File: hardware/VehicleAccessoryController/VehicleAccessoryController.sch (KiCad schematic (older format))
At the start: 70 parts, among them J501 Input, J502 Front Conn, J503 Rear Conn, J504 Left Conn, J505 Right Conn, J506 USB_B_Mini, P601 TC2030-MCP, Q201 BSS138, Q202 BSS138, Q203 BSS138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

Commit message: schematic updates
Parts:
- added C812, C813: 0.1uF, VehicleAccessoryController:C_0603, symbol Device:C
- added U106: Si8621BB-B-IS, Package_SO:SOIC-8_3.9x4.9mm_P1.27mm, symbol VehicleAccessoryController:Si8621BB-B-IS
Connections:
- net +5V: now also C813.1, U106.8 (VDD2)
- net CTRL: now also SW301.2 (B)
- net GND: now also C813.2, U106.5 (GND2); no longer C810.2, D605.1 (A), J506.5 (GND), R727.1, R732.1, U105.2 (GND), U105.25 (GND)
- net VDD: now also C812.1, U106.1 (VDD1)
- net CP2102N_RXD: now reaches U105.20 (RXD)
- net CP2102N_RXD: now also U106.3 (A2)
- net UART_RXD renamed 328P_RXD
- net 328P_RXD: now also U106.7 (B1); no longer U105.21 (TXD)
- net UART_TXD renamed 328P_TXD
- net 328P_TXD: now also U106.6 (B2)
- new net CP2102N_TXD: U105.21 (TXD), U106.2 (A1)
- new net GNDD: C810.2, C812.2, D605.1 (A), J506.5 (GND), R727.1, R732.1, U105.2 (GND), U105.25 (GND), U106.4 (GND1)
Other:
- moved on the sheet: C802, C803, C810, C811, D605, J506, P601, R702, R705, R727, R728, R731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

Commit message: test board schematic/layout updates, gerbers
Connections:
- net GND: no longer C806.2, C807.2, C808.2, C809.2
- net GNDD: now also C806.2, C807.2, C808.2, C809.2
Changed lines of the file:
@@
 Sheet 1 1
 Title "Vehicle Accessory Controller"
-Date "2019-10-31"
+Date "2019-11-15"
 Rev "0.1"
 Comp "Noctivore"
@@
 	1    0    0    -1
 $EndComp
-$Comp
-L power:GND #PWR0149
-U 1 1 5DC4B377
-P 4450 7275
-F 0 "#PWR0149" H 4450 7025 50  0001 C CNN
-F 1 "GND" H 4455 7102 50  0000 C CNN
-F 2 "" H 4450 7275 50  0001 C CNN
-F 3 "" H 4450 7275 50  0001 C CNN
-	1    4450 7275
-	1    0    0    -1
-$EndComp
-$Comp
-L power:GND #PWR0150
-U 1 1 5DC546B1
-P 4900 7275
-F 0 "#PWR0150" H 4900 7025 50  0001 C CNN
-F 1 "GND" H 4905 7102 50  0000 C CNN
-F 2 "" H 4900 7275 50  0001 C CNN
-F 3 "" H 4900 7275 50  0001 C CNN
-	1    4900 7275
-	1    0    0    -1
-$EndComp
 Wire Wire Line
 	4450 6825 4450 6900
@@
 F 3 "" H 5850 6825 50  0001 C CNN
 	1    5850 6825
-	1    0    0    -1
-$EndComp
-$Comp
-L power:GND #PWR0154
-U 1 1 5DCBD7D2
-P 5400 7275
-F 0 "#PWR0154" H 5400 7025 50  0001 C CNN
-F 1 "GND" H 5405 7102 50  0000 C CNN
-F 2 "" H 5400 7275 50  0001 C CNN
-F 3 "" H 5400 7275 50  0001 C CNN
-	1    5400 7275
-	1    0    0    -1
-$EndComp
-$Comp
-L power:GND #PWR0155
-U 1 1 5DCBD7D8
-P 5850 7275
-F 0 "#PWR0155" H 5850 7025 50  0001 C CNN
-F 1 "GND" H 5855 7102 50  0000 C CNN
-F 2 "" H 5850 7275 50  0001 C CNN
-F 3 "" H 5850 7275 50  0001 C CNN
-	1    5850 7275
 	1    0    0    -1
 $EndComp
@@
 Wire Wire Line
 	3500 1850 3500 1925
+$Comp
+L power:GNDD #PWR0149
+U 1 1 5DD0CEEA
+P 4450 7275
+F 0 "#PWR0149" H 4450 7025 50  0001 C CNN
+F 1 "GNDD" H 4454 7120 50  0000 C CNN
+F 2 "" H 4450 7275 50  0001 C CNN
+F 3 "" H 4450 7275 50  0001 C CNN
+	1    4450 7275
+	1    0    0    -1
+$EndComp
+$Comp
+L power:GNDD #PWR0150
+U 1 1 5DD13D48
+P 4900 7275
+F 0 "#PWR0150" H 4900 7025 50  0001 C CNN
+F 1 "GNDD" H 4904 7120 50  0000 C CNN
+F 2 "" H 4900 7275 50  0001 C CNN
+F 3 "" H 4900 7275 50  0001 C CNN
+	1    4900 7275
+	1    0    0    -1
+$EndComp
+$Comp
+L power:GNDD #PWR0154
+U 1 1 5DD1425B
+P 5400 7275
+F 0 "#PWR0154" H 5400 7025 50  0001 C CNN
+F 1 "GNDD" H 5404 7120 50  0000 C CNN
+F 2 "" H 5400 7275 50  0001 C CNN
+F 3 "" H 5400 7275 50  0001 C CNN
+	1    5400 7275
+	1    0    0    -1
+$EndComp
+$Comp
+L power:GNDD #PWR0155
+U 1 1 5DD1473A
+P 5850 7275
+F 0 "#PWR0155" H 5850 7025 50  0001 C CNN
+F 1 "GNDD" H 5854 7120 50  0000 C CNN
+F 2 "" H 5850 7275 50  0001 C CNN
+F 3 "" H 5850 7275 50  0001 C CNN
+	1    5850 7275
+	1    0    0    -1
+$EndComp
 $EndSCHEMATC

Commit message: BOM update, change output connectors
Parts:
- J502, J503, J504, J505: footprint VehicleAccessoryController:Keystone_8719 -> VehicleAccessoryController:TE_1776275-3
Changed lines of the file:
@@
 F 0 "J502" H 10050 1250 50  0000 L CNN
 F 1 "Front Conn" V 10275 850 50  0000 L CNN
-F 2 "VehicleAccessoryController:Keystone_8719" H 10175 1050 50  0001 C CNN
+F 2 "VehicleAccessoryController:TE_1776275-3" H 10175 1050 50  0001 C CNN
 F 3 "~" H 10175 1050 50  0001 C CNN
 	1    10175 1050
@@
 F 0 "J503" H 10050 2750 50  0000 L CNN
 F 1 "Rear Conn" V 10275 2375 50  0000 L CNN
-F 2 "VehicleAccessoryController:Keystone_8719" H 10175 2550 50  0001 C CNN
+F 2 "VehicleAccessoryController:TE_1776275-3" H 10175 2550 50  0001 C CNN
 F 3 "~" H 10175 2550 50  0001 C CNN
 	1    10175 2550
@@
 F 0 "J504" H 10050 4250 50  0000 L CNN
 F 1 "Left Conn" V 10275 3875 50  0000 L CNN
-F 2 "VehicleAccessoryController:Keystone_8719" H 10175 4050 50  0001 C CNN
+F 2 "VehicleAccessoryController:TE_1776275-3" H 10175 4050 50  0001 C CNN
 F 3 "~" H 10175 4050 50  0001 C CNN
 	1    10175 4050
@@
 F 0 "J505" H 10050 5750 50  0000 L CNN
 F 1 "Right Conn" V 10275 5325 50  0000 L CNN
-F 2 "VehicleAccessoryController:Keystone_8719" H 10175 5550 50  0001 C CNN
+F 2 "VehicleAccessoryController:TE_1776275-3" H 10175 5550 50  0001 C CNN
 F 3 "~" H 10175 5550 50  0001 C CNN
 	1    10175 5550

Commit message: schematic updates, begin layout
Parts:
- J506: symbol Connector:USB_B_Mini -> VehicleAccessoryController:USB_Mini-B
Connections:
- net +5V: no longer C802.1, C805.1, C813.1, D601.2 (A), D602.2 (A), P601.1 (MCLR/Vpp), R702.1, R726.1, U102.18 (AVCC), U102.4 (VCC), U104.8 (VDD), U106.8 (VDD2)
- net SHIELD: now also J506.0 (Shield); no longer J506.6 (Shield)
- new net +5VD: C802.1, C805.1, C813.1, D601.2 (A), D602.2 (A), P601.1 (MCLR/Vpp), R702.1, R726.1, U102.18 (AVCC), U102.4 (VCC), U104.8 (VDD), U106.8 (VDD2)
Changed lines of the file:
@@
 EESchema Schematic File Version 4
-LIBS:VehicleAccessoryController-cache
 EELAYER 30 0
 EELAYER END
@@
 Sheet 1 1
 Title "Vehicle Accessory Controller"
-Date "2019-11-15"
+Date "2019-11-20"
 Rev "0.1"
 Comp "Noctivore"
@@
 	1    0    0    -1
 $EndComp
-$Comp
-L power:+5V #PWR0103
-U 1 1 5DAF83B3
-P 5675 775
-F 0 "#PWR0103" H 5675 625 50  0001 C CNN
-F 1 "+5V" H 5690 948 50  0000 C CNN
-F 2 "" H 5675 775 50  0001 C CNN
-F 3 "" H 5675 775 50  0001 C CNN
-	1    5675 775
-	1    0    0    -1
-$EndComp
 Text Label 6525 2075 0    50   ~ 0
 328P_MOSI
@@
 	1    0    0    -1
 $EndComp
-$Comp
-L power:+5V #PWR0104
-U 1 1 5DAF8DA2
-P 4825 1175
-F 0 "#PWR0104" H 4825 1025 50  0001 C CNN
-F 1 "+5V" H 4840 1348 50  0000 C CNN
-F 2 "" H 4825 1175 50  0001 C CNN
-F 3 "" H 4825 1175 50  0001 C CNN
-	1    4825 1175
-	1    0    0    -1
-$EndComp
 Wire Wire Line
 	4825 1175 4825 1275
@@
 Wire Wire Line
 	4825 1775 4975 1775
-$Comp
-L power:+5V #PWR0105
-U 1 1 5DAF8FC6
-P 4525 1175
-F 0 "#PWR0105" H 4525 1025 50  0001 C CNN
-F 1 "+5V" H 4540 1348 50  0000 C CNN
-F 2 "" H 4525 1175 50  0001 C CNN
-F 3 "" H 4525 1175 50  0001 C CNN
-	1    4525 1175
-	1    0    0    -1
-$EndComp
 Wire Wire Line
 	4525 1175 4525 1875
@@
 F 3 "~" H 4225 1425 50  0001 C CNN
 	1    4225 1425
-	1    0    0    -1
-$EndComp
-$Comp
-L power:+5V #PWR0107
-U 1 1 5DAF9C6A
-P 4225 1175
-F 0 "#PWR0107" H 4225 1025 50  0001 C CNN
-F 1 "+5V" H 4240 1348 50  0000 C CNN
-F 2 "" H 4225 1175 50  0001 C CNN
-F 3 "" H 4225 1175 50  0001 C CNN
-	1    4225 1175
 	1    0    0    -1
 $EndComp
@@
 $EndComp
 $Comp
-L power:+5V #PWR05
-U 1 1 5DB32CA0
-P 2175 6825
-F 0 "#PWR05" H 2175 6675 50  0001 C CNN
-F 1 "+5V" H 2190 6998 50  0000 C CNN
-F 2 "" H 2175 6825 50  0001 C CNN
-F 3 "" H 2175 6825 50  0001 C CNN
-	1    2175 6825
-	1    0    0    -1
-$EndComp
-$Comp
 L Device:R R706
 U 1 1 5DB32F81
@@
 $EndComp
 $Comp
-L power:+5V #PWR0130
-U 1 1 5DB94CF1
-P 2425 5525
-F 0 "#PWR0130" H 2425 5375 50  0001 C CNN
-F 1 "+5V" H 2440 5698 50  0000 C CNN
-F 2 "" H 2425 5525 50  0001 C CNN
-F 3 "" H 2425 5525 50  0001 C CNN
-	1    2425 5525
-	1    0    0    -1
-$EndComp
-$Comp
 L power:GND #PWR0131
 U 1 1 5DB94D36
@@
 F 3 "~" H 1875 7450 50  0001 C CNN
 	1    1875 7450
-	1    0    0    -1
-$EndComp
-$Comp
-L power:+5V #PWR0140
-U 1 1 5DC8A8AF
-P 2175 7375
-F 0 "#PWR0140" H 2175 7225 50  0001 C CNN
-F 1 "+5V" H 2190 7548 50  0000 C CNN
-F 2 "" H 2175 7375 50  0001 C CNN
-F 3 "" H 2175 7375 50  0001 C CNN
-	1    2175 7375
 	1    0    0    -1
 $EndComp
@@
 	6925 1325 6925 1400
 $Comp
-L Connector:USB_B_Mini J506
+L VehicleAccessoryController:USB_Mini-B J506
 U 1 1 5DC3DA46
 P 5100 5775
@@
 $EndComp
 $Comp
-L power:+5V #PWR0144
-U 1 1 5DC3FCB0
-P 3525 5525
-F 0 "#PWR0144" H 3525 5375 50  0001 C CNN
-F 1 "+5V" H 3540 5698 50  0000 C CNN
-F 2 "" H 3525 5525 50  0001 C CNN
-F 3 "" H 3525 5525 50  0001 C CNN
-	1    3525 5525
-	1    0    0    -1
-$EndComp
-$Comp
 L power:GND #PWR0145
 U 1 1 5DC3FCB6
@@
 Wire Wire Line
 	3525 5900 3525 5975
-$Comp
-L power:+5V #PWR0146
-U 1 1 5DC61045
-P 3075 5525
-F 0 "#PWR0146" H 3075 5375 50  0001 C CNN
-F 1 "+5V" H 3090 5698 50  0000 C CNN
-F 2 "" H 3075 5525 50  0001 C CNN
-F 3 "" H 3075 5525 50  0001 C CNN
-	1    3075 5525
-	1    0    0    -1
-$EndComp
 Wire Wire Line
 	3075 5600 3075 5525
@@
 $EndComp
 $Comp
-L power:+5V #PWR0158
-U 1 1 5DD3D68A
-P 6800 3700
-F 0 "#PWR0158" H 6800 3550 50  0001 C CNN
-F 1 "+5V" H 6815 3873 50  0000 C CNN
-F 2 "" H 6800 3700 50  0001 C CNN
-F 3 "" H 6800 3700 50  0001 C CNN
-	1    6800 3700
-	1    0    0    -1
-$EndComp
-$Comp
 L power:GNDD #PWR0159
 U 1 1 5DD484EB
@@
 $EndComp
 $Comp
-L power:+5V #PWR0173
-U 1 1 5DD89F10
-P 7325 3700
-F 0 "#PWR0173" H 7325 3550 50  0001 C CNN
-F 1 "+5V" H 7340 3873 50  0000 C CNN
-F 2 "" H 7325 3700 50  0001 C CNN
-F 3 "" H 7325 3700 50  0001 C CNN
-	1    7325 3700
-	1    0    0    -1
-$EndComp
-$Comp
 L power:GND #PWR0174
 U 1 1 5DD89F1A
@@
 	1    0    0    -1
 $EndComp
+$Comp
+L power:+5VD #PWR0103
+U 1 1 5DDD65F9
+P 7575 2200
+F 0 "#PWR0103" H 7575 2050 50  0001 C CNN
+F 1 "+5VD" H 7590 2373 50  0000 C CNN
+F 2 "" H 7575 2200 50  0001 C CNN
+F 3 "" H 7575 2200 50  0001 C CNN
+	1    7575 2200
+	1    0    0    -1
+$EndComp
+$Comp
+L power:+5V #PWR0104
+U 1 1 5DDD6A05
+P 7350 2200
+F 0 "#PWR0104" H 7350 2050 50  0001 C CNN
+F 1 "+5V" H 7365 2373 50  0000 C CNN
+F 2 "" H 7350 2200 50  0001 C CNN
+F 3 "" H 7350 2200 50  0001 C CNN
+	1    7350 2200
+	1    0    0    -1
+$EndComp
+$Comp
+L power:+5VD #PWR0105
+U 1 1 5DDD71B1
+P 4225 1175
+F 0 "#PWR0105" H 4225 1025 50  0001 C CNN
+F 1 "+5VD" H 4240 1348 50  0000 C CNN
+F 2 "" H 4225 1175 50  0001 C CNN
+F 3 "" H 4225 1175 50  0001 C CNN
+	1    4225 1175
+	1    0    0    -1
+$EndComp
+$Comp
+L power:+5VD #PWR0107
+U 1 1 5DDD7521
+P 4525 1175
+F 0 "#PWR0107" H 4525 1025 50  0001 C CNN
+F 1 "+5VD" H 4540 1348 50  0000 C CNN
+F 2 "" H 4525 1175 50  0001 C CNN
+F 3 "" H 4525 1175 50  0001 C CNN
+	1    4525 1175
+	1    0    0    -1
+$EndComp
+$Comp
+L power:+5VD #PWR0130
+U 1 1 5DDD788E
+P 4825 1175
+F 0 "#PWR0130" H 4825 1025 50  0001 C CNN
+F 1 "+5VD" H 4840 1348 50  0000 C CNN
+F 2 "" H 4825 1175 50  0001 C CNN
+F 3 "" H 4825 1175 50  0001 C CNN
+	1    4825 1175
+	1    0    0    -1
+$EndComp
+$Comp
+L power:+5VD #PWR0140
+U 1 1 5DDD7BAE
+P 5675 775
+F 0 "#PWR0140" H 5675 625 50  0001 C CNN
+F 1 "+5VD" H 5690 948 50  0000 C CNN
+F 2 "" H 5675 775 50  0001 C CNN
+F 3 "" H 5675 775 50  0001 C CNN
+	1    5675 775
+	1    0    0    -1
+$EndComp
+$Comp
+L power:+5VD #PWR0144
+U 1 1 5DDE8D2C
+P 7325 3700
+F 0 "#PWR0144" H 7325 3550 50  0001 C CNN
+F 1 "+5VD" H 7340 3873 50  0000 C CNN
+F 2 "" H 7325 3700 50  0001 C CNN
+F 3 "" H 7325 3700 50  0001 C CNN
+	1    7325 3700
+	1    0    0    -1
+$EndComp
+$Comp
+L power:+5VD #PWR0146
+U 1 1 5DDEA530
+P 6800 3700
+F 0 "#PWR0146" H 6800 3550 50  0001 C CNN
+F 1 "+5VD" H 6815 3873 50  0000 C CNN
+F 2 "" H 6800 3700 50  0001 C CNN
+F 3 "" H 6800 3700 50  0001 C CNN
+	1    6800 3700
+	1    0    0    -1
+$EndComp
+$Comp
+L power:+5VD #PWR0158
+U 1 1 5DDF1341
+P 2425 5525
+F 0 "#PWR0158" H 2425 5375 50  0001 C CNN
+F 1 "+5VD" H 2440 5698 50  0000 C CNN
+F 2 "" H 2425 5525 50  0001 C CNN
+F 3 "" H 2425 5525 50  0001 C CNN
+	1    2425 5525
+	1    0    0    -1
+$EndComp
+$Comp
+L power:+5VD #PWR0173
+U 1 1 5DDF3D8B
+P 3075 5525
+F 0 "#PWR0173" H 3075 5375 50  0001 C CNN
+F 1 "+5VD" H 3090 5698 50  0000 C CNN
+F 2 "" H 3075 5525 50  0001 C CNN
+F 3 "" H 3075 5525 50  0001 C CNN
+	1    3075 5525
+	1    0    0    -1
+$EndComp
+$Comp
+L power:+5VD #PWR0177
+U 1 1 5DDF3FF7
+P 3525 5525
+F 0 "#PWR0177" H 3525 5375 50  0001 C CNN
+F 1 "+5VD" H 3540 5698 50  0000 C CNN
+F 2 "" H 3525 5525 50  0001 C CNN
+F 3 "" H 3525 5525 50  0001 C CNN
+	1    3525 5525
+	1    0    0    -1
+$EndComp
+$Comp
+L power:GND #PWR0178
+U 1 1 5DDF795F
+P 7475 2325
+F 0 "#PWR0178" H 7475 2075 50  0001 C CNN
+F 1 "GND" H 7480 2152 50  0000 C CNN
+F 2 "" H 7475 2325 50  0001 C CNN
+F 3 "" H 7475 2325 50  0001 C CNN
+	1    7475 2325
+	1    0    0    -1
+$EndComp
+$Comp
+L power:+5VD #PWR0179
+U 1 1 5DE325F0
+P 2175 6825
+F 0 "#PWR0179" H 2175 6675 50  0001 C CNN
+F 1 "+5VD" H 2190 6998 50  0000 C CNN
+F 2 "" H 2175 6825 50  0001 C CNN
+F 3 "" H 2175 6825 50  0001 C CNN
+	1    2175 6825
+	1    0    0    -1
+$EndComp
+$Comp
+L power:+5VD #PWR0180
+U 1 1 5DE3C0EE
+P 2175 7375
+F 0 "#PWR0180" H 2175 7225 50  0001 C CNN
+F 1 "+5VD" H 2190 7548 50  0000 C CNN
+F 2 "" H 2175 7375 50  0001 C CNN
+F 3 "" H 2175 7375 50  0001 C CNN
+	1    2175 7375
+	1    0    0    -1
+$EndComp

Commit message: test board PDFs, label updates, merge duplicates on BOMs
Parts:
- R731: value 22.1k -> 22k1
- R732: value 47.5k -> 47k5
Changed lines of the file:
@@
 Sheet 1 1
 Title "Vehicle Accessory Controller"
-Date "2019-11-20"
+Date "2019-11-22"
 Rev "0.1"
 Comp "Noctivore"
@@
 	5400 5575 5400 5475
 NoConn ~ 5400 5975
-$Comp
-L Device:R R732
-U 1 1 5DF513E5
-P 3775 4500
-F 0 "R732" H 3850 4450 50  0000 L CNN
-F 1 "47.5k" H 3850 4550 50  0000 L CNN
-F 2 "VehicleAccessoryController:R_0603" V 3705 4500 50  0001 C CNN
-F 3 "~" H 3775 4500 50  0001 C CNN
-	1    3775 4500
-	-1   0    0    1
-$EndComp
 Wire Wire Line
 	3775 4650 3775 4725
@@
 P 3775 4100
 F 0 "R731" H 3850 4050 50  0000 L CNN
-F 1 "22.1k" H 3850 4150 50  0000 L CNN
+F 1 "22k1" H 3850 4150 50  0000 L CNN
 F 2 "VehicleAccessoryController:R_0603" V 3705 4100 50  0001 C CNN
 F 3 "~" H 3775 4100 50  0001 C CNN
@@
 	1    0    0    -1
 $EndComp
+$Comp
+L Device:R R732
+U 1 1 5DF513E5
+P 3775 4500
+F 0 "R732" H 3850 4450 50  0000 L CNN
+F 1 "47k5" H 3850 4550 50  0000 L CNN
+F 2 "VehicleAccessoryController:R_0603" V 3705 4500 50  0001 C CNN
+F 3 "~" H 3775 4500 50  0001 C CNN
+	1    3775 4500
+	-1   0    0    1
+$EndComp
 $EndSCHEMATC

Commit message: shcematic updates
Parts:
- removed U106: Si8621BB-B-IS, Package_SO:SOIC-8_3.9x4.9mm_P1.27mm, symbol VehicleAccessoryController:Si8621BB-B-IS
- added C814, C815: 1uF, VehicleAccessoryController:C_0603, symbol Device:C
- added U106: Si8631EC-B-IS1, Package_SO:SOIC-16_3.9x9.9mm_P1.27mm, symbol VehicleAccessoryController:Si8631EC-B-IS1
- added U107: NCV551SN50T1G, Package_TO_SOT_SMD:SOT-23-5, symbol VehicleAccessoryController:NCV551SN50T1G
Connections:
- net +5V: now also C814.1, U107.1 (IN), U107.3 (EN)
- net +5VD: now also C815.1, U106.10 (EN2), U106.16 (VDD2), U107.5 (OUT)
- net 328P_RXD: now also U106.13 (B2)
- net 328P_TXD: now also U106.12 (B3)
- net CP2102N_RXD: now also U106.5 (A3)
- net CP2102N_TXD: now also U106.4 (A2)
- net GND: now also C814.2, C815.2, U106.15 (GND2), U106.9 (GND2), U107.2 (GND)
- net GNDD: now also U106.2 (GND1), U106.8 (GND1)
- net VDD: now also U106.1 (VDD1), U106.7 (EN1)
- net at C811.2: now also U106.14 (B1); no longer U105.23 (DTR)
- net 328P_RESET renamed 328P_RST
- net 328P_SS: no longer names the net of U102.14 (PB2(SS))
- new net CP2102N_RST: U105.23 (DTR), U106.3 (A1)
- no-connect marks 13 -> 14
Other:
- moved on the sheet: C811, C813

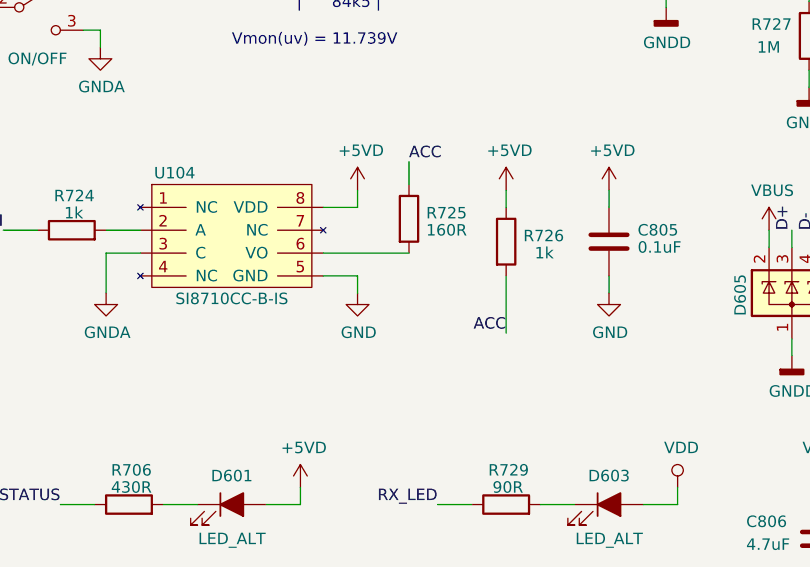
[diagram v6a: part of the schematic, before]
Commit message: correct fuse holder, ACC pull-up, BOM Accessories, create firmware dir
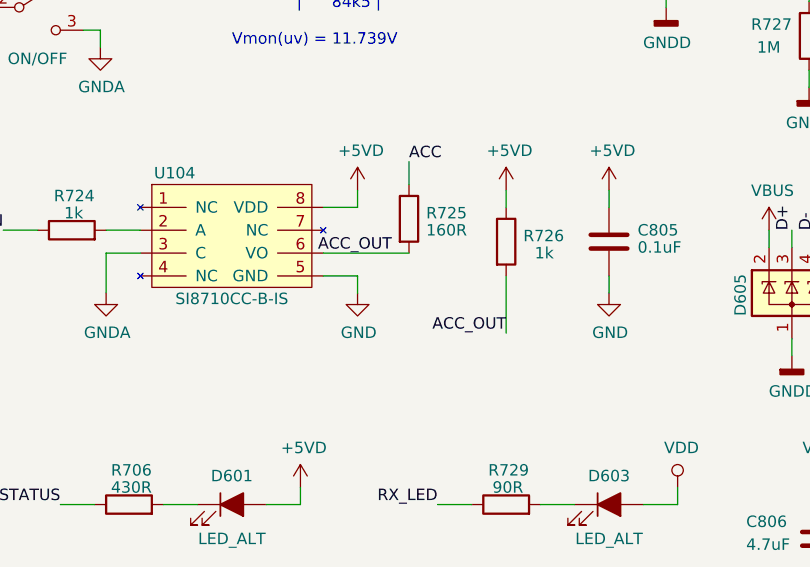
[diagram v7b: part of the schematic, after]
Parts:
- F401: footprint VehicleAccessoryController:Littelfuse_01530007 -> VehicleAccessoryController:Keystone_3587
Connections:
- net ACC: no longer R726.2
- net ACC_OUT: now reaches R725.2, U104.6 (VO)
- net ACC_OUT: now also R726.2
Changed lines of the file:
@@
 Sheet 1 1
 Title "Vehicle Accessory Controller"
-Date "2019-11-23"
+Date "2019-11-29"
 Rev "0.1"
 Comp "Noctivore"
@@
 F 0 "F401" V 1200 825 50  0000 L CNN
 F 1 "Fuse" V 1125 825 50  0000 L CNN
-F 2 "VehicleAccessoryController:Littelfuse_01530007" V 980 900 50  0001 C CNN
+F 2 "VehicleAccessoryController:Keystone_3587" V 980 900 50  0001 C CNN
 F 3 "~" H 1050 900 50  0001 C CNN
 	1    1050 900
@@
 ACC
 Text Label 3075 6150 2    50   ~ 0
-ACC
+ACC_OUT
 $Comp
 L Device:R R725
@@
 Wire Wire Line
 	7000 3600 7150 3600
+Text Label 2575 5800 2    50   ~ 0
+ACC_OUT
 $EndSCHEMATC

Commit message: layout updates
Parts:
- added H1, H2: Mounting_Hole, VehicleAccessoryController:Mounting_Hole, symbol Mechanical:MountingHole_Pad
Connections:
- net GNDA: now also H1.1, H2.1
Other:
- moved on the sheet: fid1, fid2, fid3
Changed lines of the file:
@@
 Sheet 1 1
 Title "Vehicle Accessory Controller"
-Date "2019-11-29"
+Date "2019-12-03"
 Rev "0.1"
 Comp "Noctivore"
@@
 L VehicleAccessoryController:FID fid1
 U 1 1 5DAF80EF
-P 7825 825
-F 0 "fid1" H 7775 975 60  0000 L CNN
-F 1 "FID" H 7775 675 60  0000 L CNN
-F 2 "VehicleAccessoryController:Fiducial" H 7825 825 60  0001 C CNN
-F 3 "" H 7825 825 60  0001 C CNN
-	1    7825 825
+P 4825 7750
+F 0 "fid1" H 4775 7900 60  0000 L CNN
+F 1 "FID" H 4775 7600 60  0000 L CNN
+F 2 "VehicleAccessoryController:Fiducial" H 4825 7750 60  0001 C CNN
+F 3 "" H 4825 7750 60  0001 C CNN
+	1    4825 7750
 	1    0    0    -1
 $EndComp
@@
 L VehicleAccessoryController:FID fid2
 U 1 1 5DB12261
-P 8175 825
-F 0 "fid2" H 8125 975 60  0000 L CNN
-F 1 "FID" H 8125 675 60  0000 L CNN
-F 2 "VehicleAccessoryController:Fiducial" H 8175 825 60  0001 C CNN
-F 3 "" H 8175 825 60  0001 C CNN
-	1    8175 825
+P 5175 7750
+F 0 "fid2" H 5125 7900 60  0000 L CNN
+F 1 "FID" H 5125 7600 60  0000 L CNN
+F 2 "VehicleAccessoryController:Fiducial" H 5175 7750 60  0001 C CNN
+F 3 "" H 5175 7750 60  0001 C CNN
+	1    5175 7750
 	1    0    0    -1
 $EndComp
@@
 L VehicleAccessoryController:FID fid3
 U 1 1 5DB12492
-P 8525 825
-F 0 "fid3" H 8475 975 60  0000 L CNN
-F 1 "FID" H 8475 675 60  0000 L CNN
-F 2 "VehicleAccessoryController:Fiducial" H 8525 825 60  0001 C CNN
-F 3 "" H 8525 825 60  0001 C CNN
-	1    8525 825
+P 5525 7750
+F 0 "fid3" H 5475 7900 60  0000 L CNN
+F 1 "FID" H 5475 7600 60  0000 L CNN
+F 2 "VehicleAccessoryController:Fiducial" H 5525 7750 60  0001 C CNN
+F 3 "" H 5525 7750 60  0001 C CNN
+	1    5525 7750
 	1    0    0    -1
 $EndComp
@@
 Text Label 2575 5800 2    50   ~ 0
 ACC_OUT
+$Comp
+L Mechanical:MountingHole_Pad H1
+U 1 1 5DFA9925
+P 7800 850
+F 0 "H1" H 7900 900 50  0000 L CNN
+F 1 "Mounting_Hole" H 7525 1025 50  0000 L CNN
+F 2 "VehicleAccessoryController:Mounting_Hole" H 7800 850 50  0001 C CNN
+F 3 "~" H 7800 850 50  0001 C CNN
+	1    7800 850
+	1    0    0    -1
+$EndComp
+$Comp
+L power:GNDA #PWR0185
+U 1 1 5DFB2820
+P 7800 975
+F 0 "#PWR0185" H 7800 725 50  0001 C CNN
+F 1 "GNDA" H 7805 802 50  0000 C CNN
+F 2 "" H 7800 975 50  0001 C CNN
+F 3 "" H 7800 975 50  0001 C CNN
+	1    7800 975
+	1    0    0    -1
+$EndComp
+$Comp
+L Mechanical:MountingHole_Pad H2
+U 1 1 5DFD86D5
+P 8500 850
+F 0 "H2" H 8300 900 50  0000 L CNN
+F 1 "Mounting_Hole" H 8225 1025 50  0000 L CNN
+F 2 "VehicleAccessoryController:Mounting_Hole" H 8500 850 50  0001 C CNN
+F 3 "~" H 8500 850 50  0001 C CNN
+	1    8500 850
+	1    0    0    -1
+$EndComp
+$Comp
+L power:GNDA #PWR0186
+U 1 1 5DFDBE49
+P 8500 975
+F 0 "#PWR0186" H 8500 725 50  0001 C CNN
+F 1 "GNDA" H 8505 802 50  0000 C CNN
+F 2 "" H 8500 975 50  0001 C CNN
+F 3 "" H 8500 975 50  0001 C CNN
+	1    8500 975
+	1    0    0    -1
+$EndComp
+Wire Wire Line
+	7800 950  7800 975
+Wire Wire Line
+	8500 950  8500 975
 $EndSCHEMATC
